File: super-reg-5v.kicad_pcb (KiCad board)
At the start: 2 copper layers, 85 x 35 mm, 45 parts, among them Q1 2SA1015, Q2 D44H11, U1 LM317T, U2 AD825, U3 AD825, X1 AC_IN, X2 DC_OUT

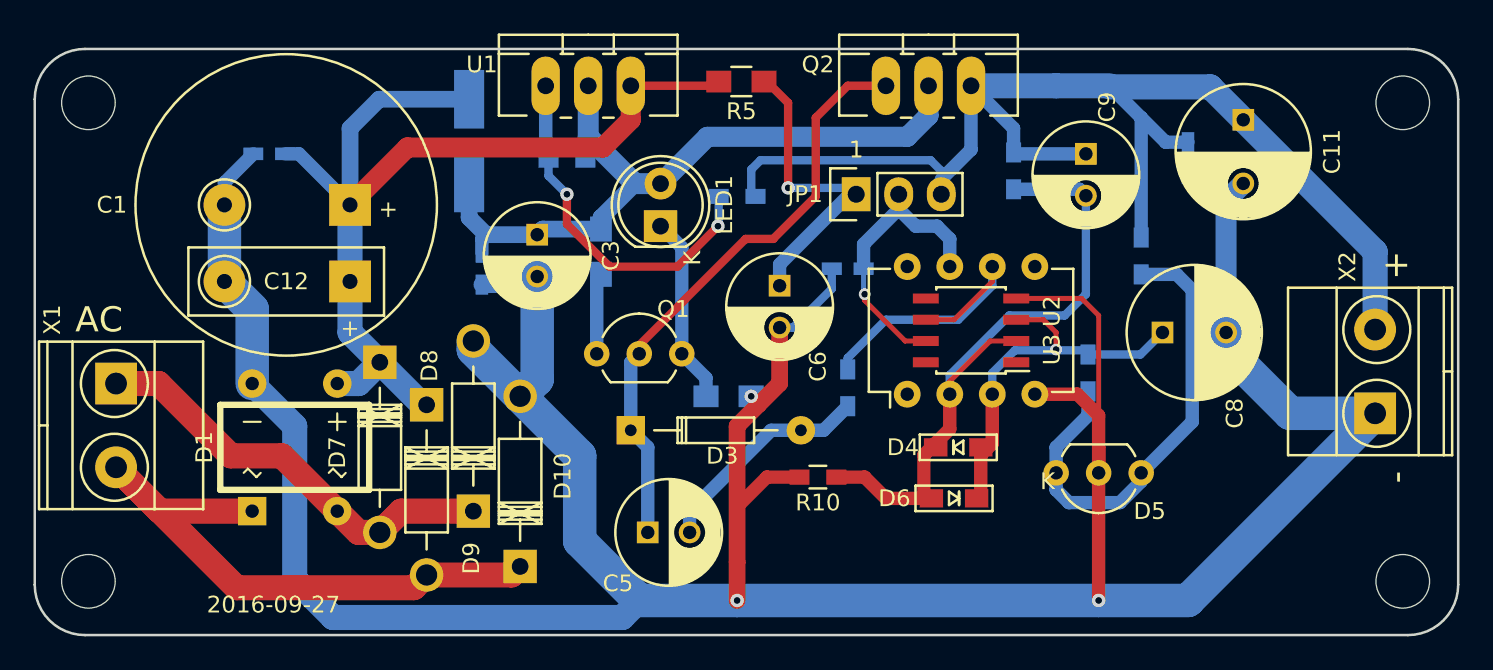
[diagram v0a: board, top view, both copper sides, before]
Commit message: change bypass Cap
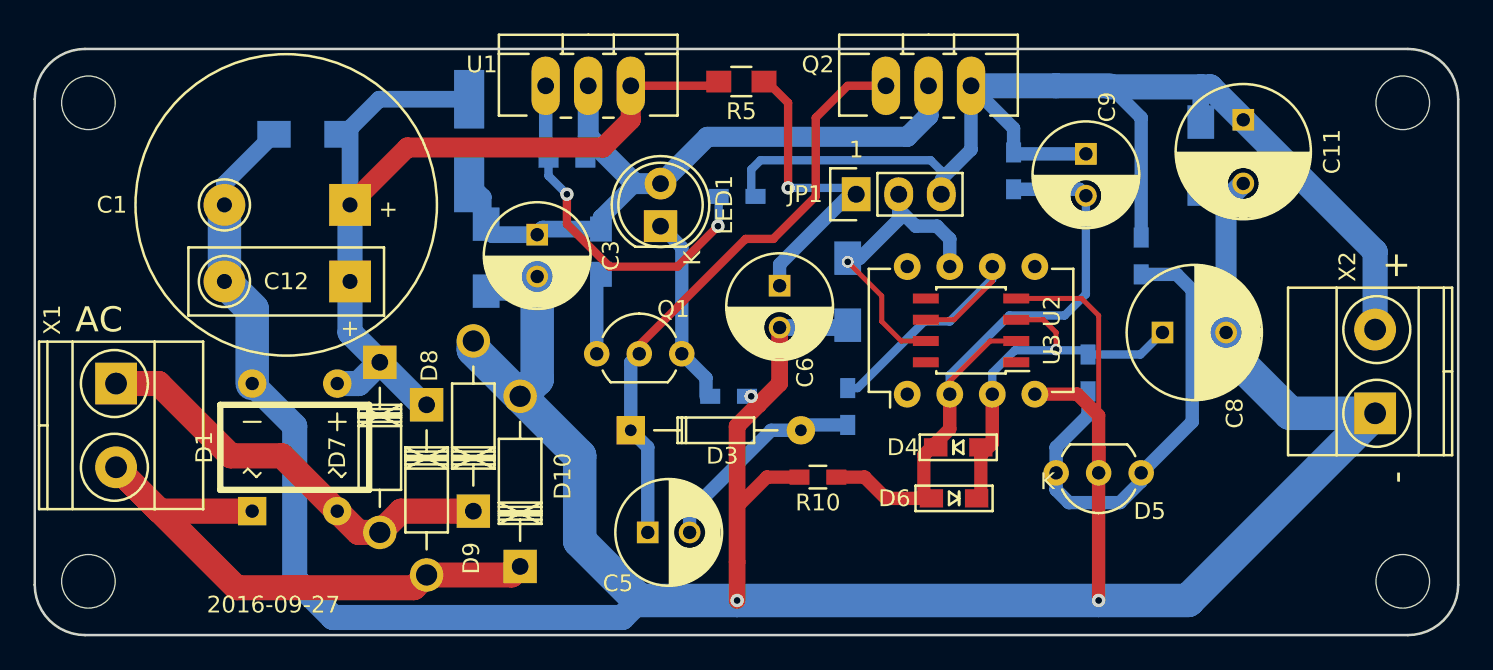
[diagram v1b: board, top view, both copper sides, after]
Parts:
- C10, C2, C4, C7: value 0.1u -> 0.1u C0G; footprint Capacitors_SMD:C_0603_HandSoldering -> Capacitors_SMD:C_1206_HandSoldering
- R3: footprint Resistors_SMD:R_0805_HandSoldering -> Resistors_SMD:R_0603_HandSoldering
- moved C2 2.57 mm to (129.3, 79.1)
- moved C7 1.37 mm to (161.5, 88.5), turned to 270 degrees
- moved R6 1.12 mm to (161.5, 95.4)
- moved C10 0.78 mm to (182.6, 80.4)
- moved C4 0.71 mm to (140.0, 86.5)
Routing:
- net Net-(C1-Pad1): track 61.6 -> 56.4 mm
- net /OPAMP_PW: track 16.4 -> 18.7 mm
- net Net-(C3-Pad1): track 44.7 -> 43.3 mm
- net Net-(C10-Pad1): track 76.2 -> 75.5 mm

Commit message: fix track width
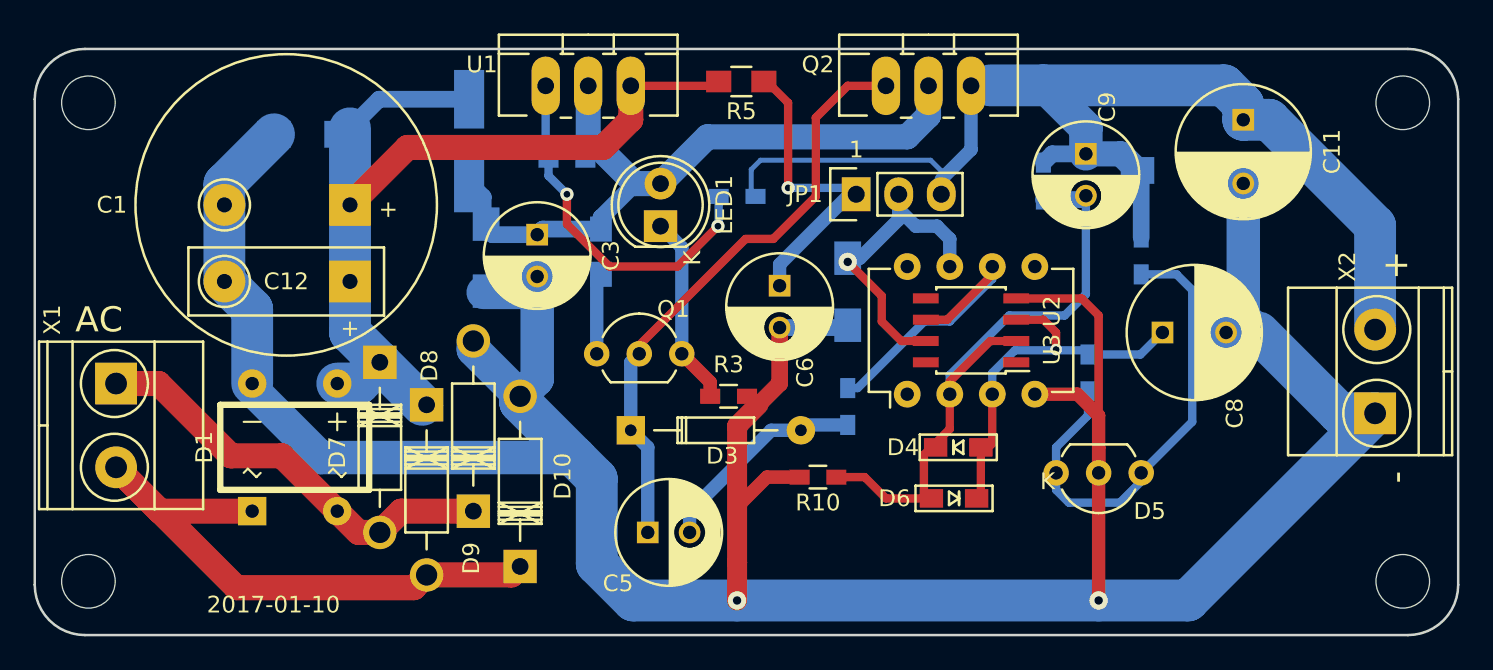
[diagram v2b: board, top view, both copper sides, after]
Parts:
- R3: moved to F.Cu
- moved C10 1.99 mm to (180.8, 81.3), turned to 0 degrees
- moved R9 1.88 mm to (173.2, 81.9)
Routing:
- net GND: track 211.6 -> 198.5 mm, vias 3 -> 2
- net Net-(C10-Pad1): track 75.5 -> 70.6 mm
- net /OPAMP_N: track 40.2 -> 38.1 mm
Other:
- board text added: "2017-01-10"
- board text removed: "2016-09-27"
